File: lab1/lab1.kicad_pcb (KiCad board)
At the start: 2 copper layers, 40 x 40 mm, 25 parts, among them J1 USB_OTG, J2 Conn_01x06_Male, U1 STM32F411RETx, U2 LM1117ADJ, Y1 8.0Mhz

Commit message: Start routing copper in lab 2
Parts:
- moved R2 76.8 mm to (113.9, 91.4), turned to 180 degrees
- moved C15 70.0 mm to (108.3, 85.1), turned to 180 degrees
- moved R1 65.9 mm to (119.4, 91.4), turned to 180 degrees
- moved C14 63.7 mm to (108.3, 80.0), turned to 180 degrees
- moved C16 62.0 mm to (109.2, 56.7), turned to 180 degrees
- moved R3 55.2 mm to (114.3, 74.9), turned to 180 degrees
- moved U2 53.8 mm to (118.8, 83.5), turned to 90 degrees
- moved R4 47.0 mm to (122.7, 66.0), turned to 180 degrees
- moved C13 32.5 mm to (126.6, 77.4), turned to 90 degrees
- moved J1 31.1 mm to (132.1, 87.6)
- moved C9 30.7 mm to (127.8, 68.3)
- moved C8 28.9 mm to (127.8, 71.1)
- moved C7 24.5 mm to (101.9, 59.5), turned to 180 degrees
- moved C6 19.0 mm to (101.9, 62.0), turned to 180 degrees
- moved J2 15.1 mm to (115.1, 55.8)
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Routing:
- net +3V3: track 0.00 -> 52.7 mm, vias 0 -> 2
- net +5V: track 0.00 -> 9.35 mm
- net Net-(R1-Pad2): track 0.00 -> 8.88 mm
- net Net-(R3-Pad2): track 0.00 -> 3.83 mm
- net GND: track 0.00 -> 0.70 mm

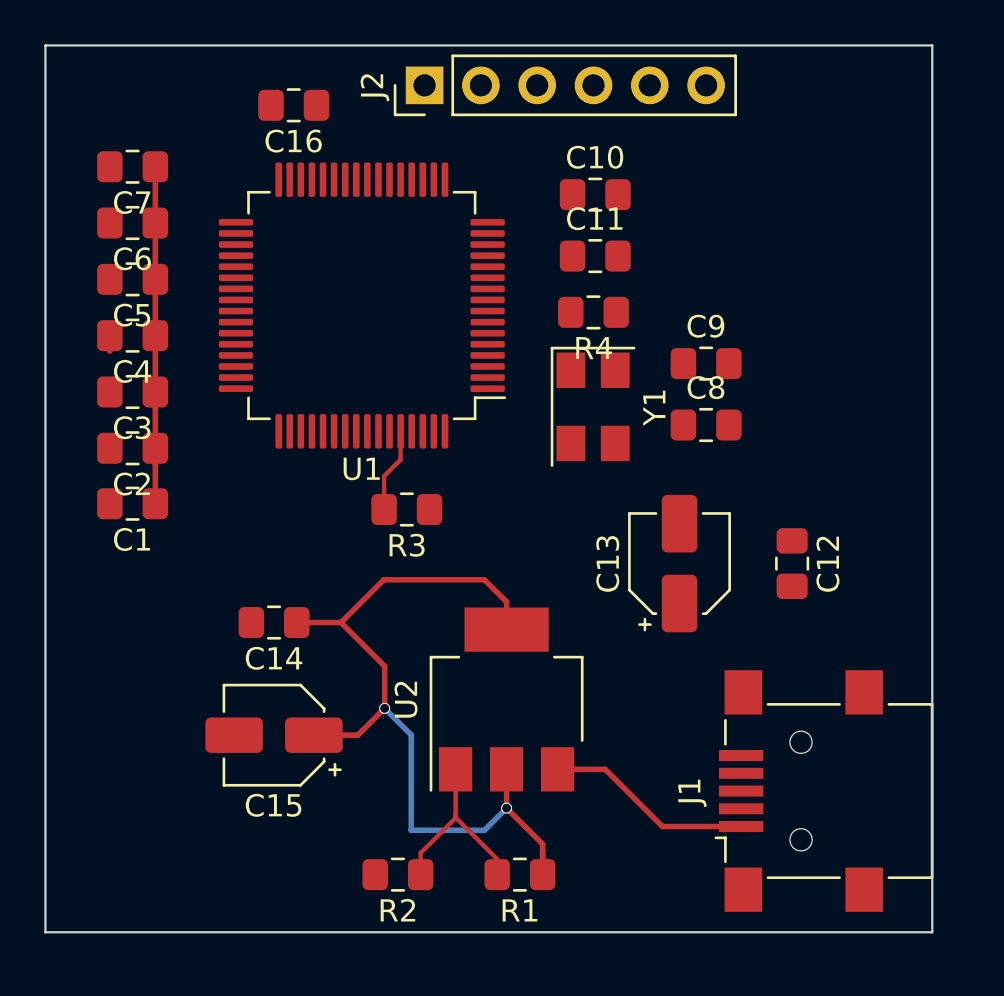
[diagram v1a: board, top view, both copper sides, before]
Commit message: Finish routing, start work on adding GND plate
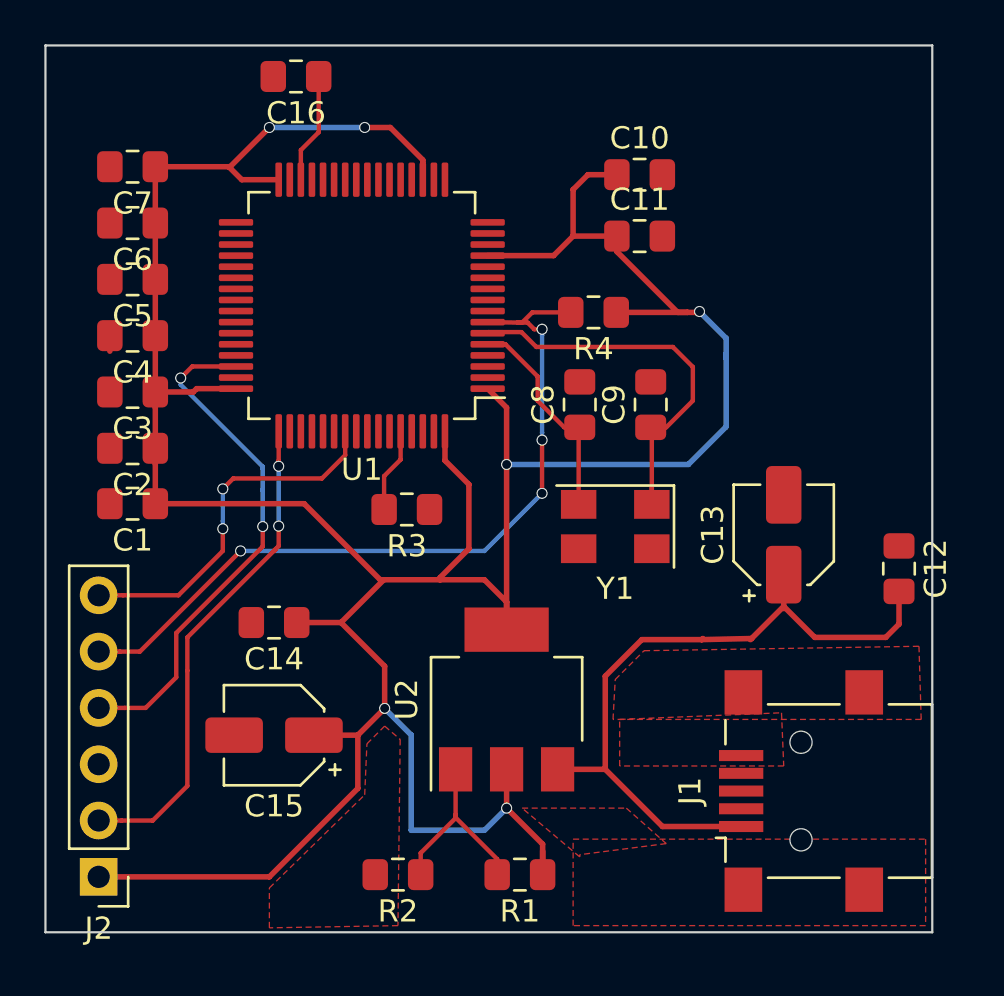
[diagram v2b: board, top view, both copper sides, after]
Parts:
- moved J2 38.6 mm to (100.4, 91.5), turned to 180 degrees
- moved C8 5.77 mm to (122.1, 70.2), turned to 90 degrees
- moved Y1 5.49 mm to (123.7, 75.7), turned to 180 degrees
- moved C13 4.88 mm to (131.3, 76.1)
- moved C12 4.83 mm to (136.5, 77.6)
- moved C9 3.11 mm to (125.3, 70.2), turned to 90 degrees
- moved C10 2.19 mm to (124.8, 59.8)
- moved C11 2.19 mm to (124.8, 62.6)
- moved C16 1.30 mm to (109.3, 55.4)
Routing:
- net +3V3: track 52.7 -> 155.4 mm, vias 2 -> 6
- net /NRST: track 0.00 -> 35.5 mm, vias 0 -> 4
- net /SWDIO: track 0.00 -> 23.5 mm, vias 0 -> 2
- net +5V: track 9.35 -> 32.1 mm
- net /SWCLK: track 0.00 -> 22.5 mm, vias 0 -> 2
- net Net-(C9-Pad1): track 0.00 -> 18.2 mm
- net /SWO: track 0.00 -> 16.5 mm, vias 0 -> 2
- net Net-(C8-Pad1): track 0.00 -> 9.84 mm
- net Net-(C16-Pad1): track 0.00 -> 4.99 mm
- added copper zone on F.Cu, net GND

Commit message: Finish lab 2
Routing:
- net GND: track 0.70 -> 14.4 mm, vias 0 -> 4
- added copper zone on B.Cu, net GND
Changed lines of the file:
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@@
     (thickness 1.6)
     (drawings 4)
-    (tracks 205)
+    (tracks 227)
     (zones 0)
     (modules 25)
@@
   (segment (start 112.4 57.7) (end 113.555682 57.7) (width 0.25) (layer F.Cu) (net 1))
   (segment (start 100.905 67.09) (end 100.905 67.79) (width 0.25) (layer F.Cu) (net 2))
+  (via (at 102.8 90.2) (size 0.5) (drill 0.4) (layers F.Cu B.Cu) (net 2))
+  (via (at 115 73.2) (size 0.5) (drill 0.4) (layers F.Cu B.Cu) (net 2))
+  (segment (start 118.12 63.98) (end 118.14 64) (width 0.25) (layer F.Cu) (net 2))
+  (segment (start 117.945 63.98) (end 118.12 63.98) (width 0.25) (layer F.Cu) (net 2))
+  (segment (start 115.52 72.68) (end 115 73.2) (width 0.25) (layer F.Cu) (net 2))
+  (segment (start 115.52 71.405) (end 115.52 72.68) (width 0.25) (layer F.Cu) (net 2))
+  (via (at 120.7 64.5) (size 0.5) (drill 0.4) (layers F.Cu B.Cu) (net 2))
+  (segment (start 120.18 63.98) (end 120.7 64.5) (width 0.25) (layer F.Cu) (net 2))
+  (segment (start 117.945 63.98) (end 120.18 63.98) (width 0.25) (layer F.Cu) (net 2))
+  (segment (start 115.52 60.055) (end 115.52 58.68) (width 0.25) (layer F.Cu) (net 2))
+  (segment (start 115.52 58.68) (end 116.6 57.6) (width 0.25) (layer F.Cu) (net 2))
+  (segment (start 109.02 60.055) (end 109.02 58.92) (width 0.25) (layer F.Cu) (net 2))
+  (segment (start 109.02 58.92) (end 108.7 58.6) (width 0.25) (layer F.Cu) (net 2))
+  (segment (start 129.07 86.03) (end 128.9 86.2) (width 0.25) (layer F.Cu) (net 2))
+  (segment (start 129.38 86.03) (end 129.07 86.03) (width 0.25) (layer F.Cu) (net 2))
+  (segment (start 128.9 86.2) (end 127 86.2) (width 0.25) (layer F.Cu) (net 2))
+  (via (at 105.1 68.9) (size 0.5) (drill 0.4) (layers F.Cu B.Cu) (net 2))
+  (segment (start 105.18 68.98) (end 105.1 68.9) (width 0.25) (layer F.Cu) (net 2))
+  (segment (start 106.595 68.98) (end 105.18 68.98) (width 0.25) (layer F.Cu) (net 2))
   (segment (start 122.05 71.275) (end 122.1 71.225) (width 0.2) (layer F.Cu) (net 3))
   (segment (start 122.05 74.7) (end 122.05 71.275) (width 0.2) (layer F.Cu) (net 3))
@@
   (segment (start 104.1 69) (end 104.1 69) (width 0.2) (layer B.Cu) (net 11))
   (via (at 104.1 69) (size 0.5) (drill 0.4) (layers F.Cu B.Cu) (net 11))
-  (segment (start 104.62 68.48) (end 106.595 68.48) (width 0.2) (layer F.Cu) (net 11))
-  (segment (start 104.1 69) (end 104.62 68.48) (width 0.2) (layer F.Cu) (net 11))
+  (segment (start 104.1 68.6) (end 104.1 69) (width 0.2) (layer F.Cu) (net 11))
+  (segment (start 104.4 68.3) (end 104.1 68.6) (width 0.2) (layer F.Cu) (net 11))
+  (segment (start 105.5 68.3) (end 104.4 68.3) (width 0.2) (layer F.Cu) (net 11))
+  (segment (start 106.595 68.48) (end 105.68 68.48) (width 0.2) (layer F.Cu) (net 11))
+  (segment (start 105.68 68.48) (end 105.5 68.3) (width 0.2) (layer F.Cu) (net 11))
   (segment (start 119.96 66.04) (end 121.695 66.04) (width 0.2) (layer F.Cu) (net 12))
   (segment (start 119.52 66.48) (end 119.96 66.04) (width 0.2) (layer F.Cu) (net 12))
@@
       )
     )
+  )
+  (zone (net 2) (net_name GND) (layer F.Cu) (hatch edge 0.508)
+    (connect_pads (clearance 0.508))
+    (min_thickness 0.254)
+    (fill yes (arc_segments 32) (thermal_gap 0.508) (thermal_bridge_width 0.508))
+    (polygon
+      (pts
+        (xy 137.5 54.3) (xy 137.7 93.6) (xy 98.5 93.7) (xy 98.3 54.2)
+      )
+    )
+  )
+  (zone (net 2) (net_name GND) (layer B.Cu) (hatch edge 0.508)
+    (connect_pads (clearance 0.508))
+    (min_thickness 0.254)
+    (fill yes (arc_segments 32) (thermal_gap 0.508) (thermal_bridge_width 0.508))
+    (polygon
+      (pts
+        (xy 137.7 93.7) (xy 98.5 93.7) (xy 98.3 54.2) (xy 137.9 54.1)
+      )
+    )
